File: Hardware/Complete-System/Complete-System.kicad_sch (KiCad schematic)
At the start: 1 part

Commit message: Not perfect or finished but functional for now
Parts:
- added C1: Start. Cap., symbol Device:C
- added D1: WS2812-Strip, LED_SMD:LED_WS2812_PLCC6_5.0x5.0mm_P1.6mm, symbol LED:WS2812
- added F1: Polyfuse, symbol Device:Polyfuse
- added J1: IEC_60320_C14_Receptacle, symbol Connector:IEC_60320_C14_Receptacle
- added J2: USB_C_Receptacle_USB2.0_14P, symbol Connector:USB_C_Receptacle_USB2.0_14P
- added M1: Int. Fan, symbol Motor:Fan_IEC-60617
- added M2: Cond. Fan, symbol Motor:Fan_IEC-60617
- added M3: Compressor, symbol Motor:Motor_AC
- added NE1: HEAT_OFF, symbol Device:Lamp_Neon
- added R1: 1KW Heater, symbol Device:Heater
- added SW1: Door Switch, symbol Switch:SW_Push_SPDT
- added TC1: Compressor, symbol Device:Thermocouple
- added TC2: Evaporator, symbol Device:Thermocouple
- added TC3: Condensor, symbol Device:Thermocouple
- added U1: SHT30-DIS, Sensor_Humidity:Sensirion_DFN-8-1EP_2.5x2.5mm_P0.5mm_EP1.1x1.7mm, symbol Sensor_Humidity:SHT30-DIS
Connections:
- net at PCB1.101-1 (LOAD_4): now also C1.1, M3.1
- net at PCB1.103-1 (N): now also C1.2, M3.2
- net at PCB1.104-1 (LOAD_3): now also F1.2
- net at PCB1.105-1 (LOAD_3_AUX): now also NE1.2
- net at PCB1.106-1 (N): now also NE1.1, R1.2
- net at PCB1.107-1 (LOAD_2): now also M2.1 (+)
- net at PCB1.108-1 (N): now also M2.2 (-)
- net at PCB1.109-1 (LOAD_1): now also M1.1 (+)
- net at PCB1.110-1 (N): now also M1.2 (-)
- net at PCB1.111-1 (AC_L): now also J1.1 (L)
- net at PCB1.112-1 (AC_N): now also J1.2 (N)
- net at PCB1.115-1 (5V): now also D1.3 (VCC), D1.5 (VDD)
- net at PCB1.115-2 (NEOPIXEL): now also D1.2 (DIN)
- net at PCB1.115-3 (GND): now also D1.6 (VSS)
- new net: U1.8 (VSS), U1.9 (VSS)
- new net: F1.1, R1.1
- new net: J2.A4 (VBUS), J2.A9 (VBUS), J2.B4 (VBUS), J2.B9 (VBUS)
- new net Earth: J1.3 (PE), J2.A1 (GND), J2.A12 (GND), J2.B1 (GND), J2.B12 (GND), J2.S1 (SHIELD)
- no-connect marks 0 -> 26
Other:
- note added: "Compressor"
- note added: "Heat"
- moved on the sheet: PCB1

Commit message: More clean
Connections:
- no-connect marks 26 -> 28
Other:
- note added: "Do not VBUS from ext. usb to controller (except for testing)"
- moved on the sheet: F1, J1, M1, M2, U1

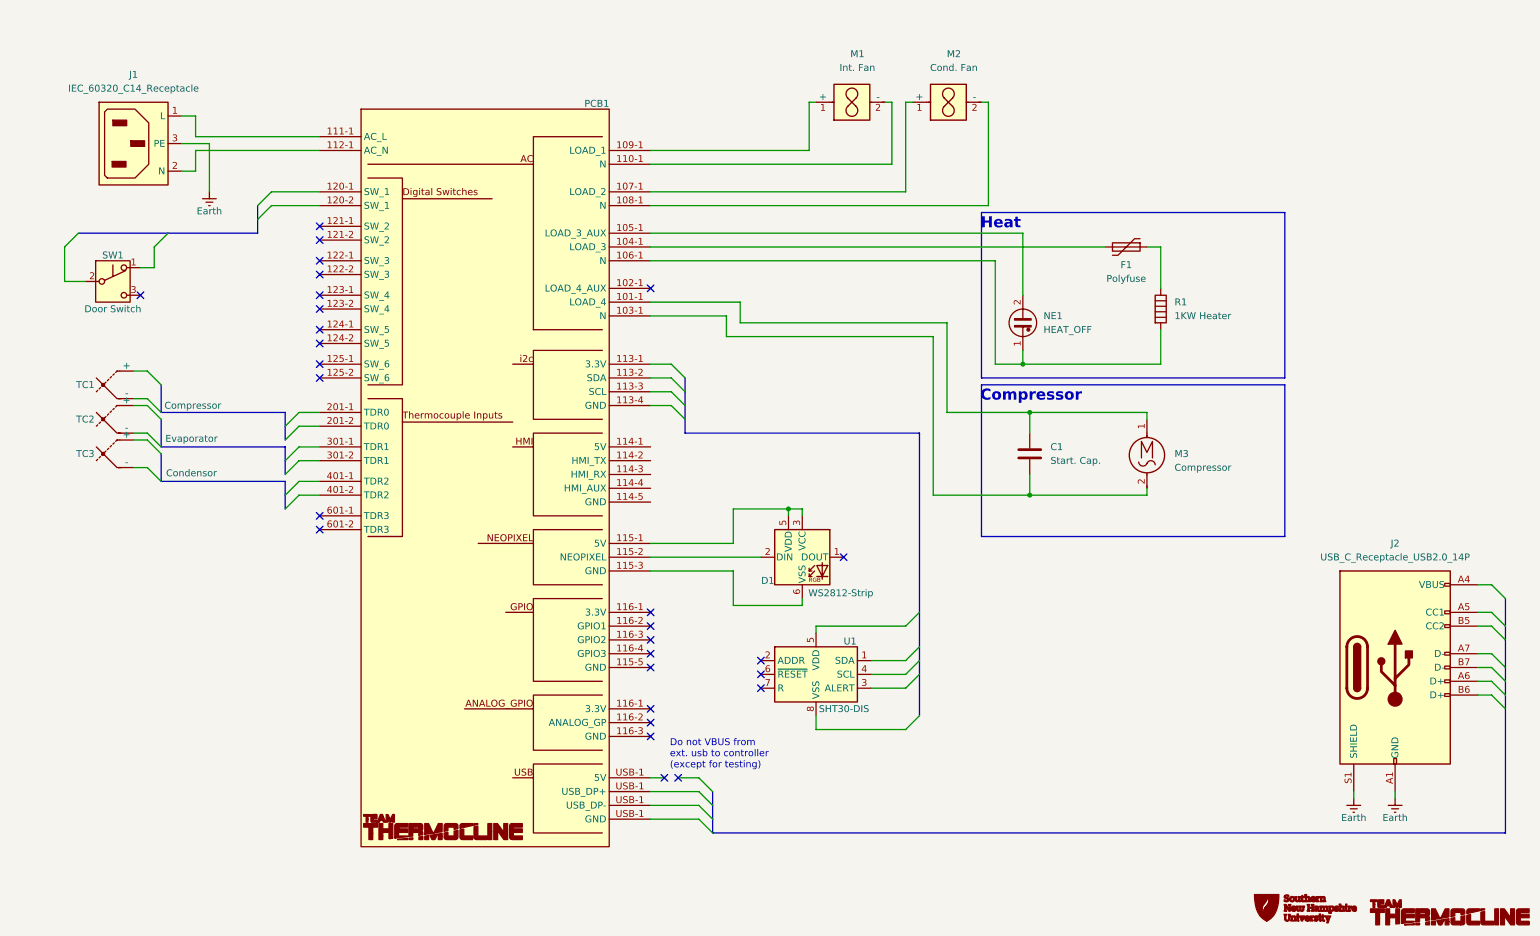
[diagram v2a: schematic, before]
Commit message: Include starter caps
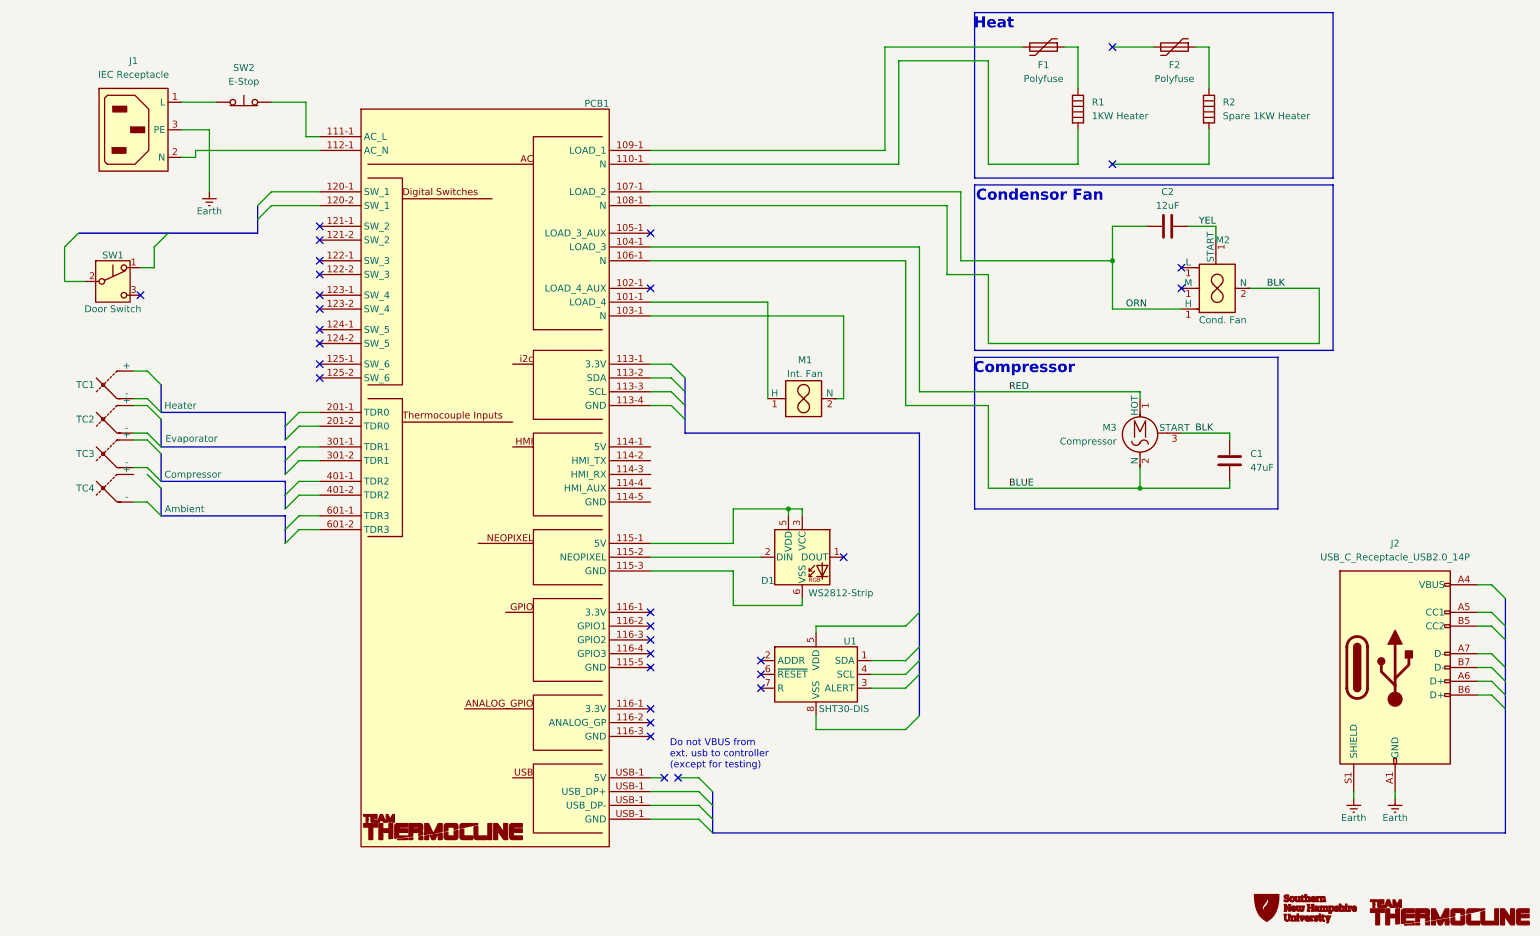
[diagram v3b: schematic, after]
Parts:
- removed NE1: HEAT_OFF, symbol Device:Lamp_Neon
- added C2: 12uF, symbol Device:C
- added F2: Polyfuse, symbol Device:Polyfuse
- added R2: Spare 1KW Heater, symbol Device:Heater
- added SW2: E-Stop, symbol Switch:SW_Push_Open
- added TC4: Ambient, symbol Device:Thermocouple
- C1: value Start. Cap. -> 47uF
- J1: value IEC_60320_C14_Receptacle -> IEC Receptacle
- PCB1: value ~ -> (none)
- TC1: value Compressor -> Heater
- TC3: value Condensor -> Compressor
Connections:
- net BLUE: now reaches C1.2, M3.2 (N)
- net BLUE: now also PCB1.106-1 (N); no longer PCB1.103-1 (N)
- net at R1.2: now also PCB1.110-1 (N); no longer PCB1.106-1 (N)
- net at J1.1 (L): now also SW2.1 (A); no longer PCB1.111-1 (AC_L)
- net at F1.2: now also PCB1.109-1 (LOAD_1); no longer PCB1.104-1 (LOAD_3)
- net at M1.1 (H): now also PCB1.101-1 (LOAD_4); no longer PCB1.109-1 (LOAD_1)
- net at M1.2 (N): now also PCB1.103-1 (N); no longer PCB1.110-1 (N)
- net ORN: now reaches M2.1 (START), PCB1.107-1 (LOAD_2)
- net ORN: now also C2.1
- net BLK: now reaches M2.2 (N), PCB1.108-1 (N)
- net BLK: now also C1.1, M3.3 (START)
- new net: F2.1, R2.1
- new net: PCB1.111-1 (AC_L), SW2.2 (B)
- new net RED: M3.1 (HOT), PCB1.104-1 (LOAD_3)
- new net YEL: C2.2, M2.1 (START)
- no-connect marks 28 -> 31
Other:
- note added: "Condensor Fan"
- company: (none) -> Team Thermocline
- title: (none) -> Temperature Chamber Complete Overview
- moved on the sheet: F1, J1, M1, R1
